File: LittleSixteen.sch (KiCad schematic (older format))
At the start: 17 parts

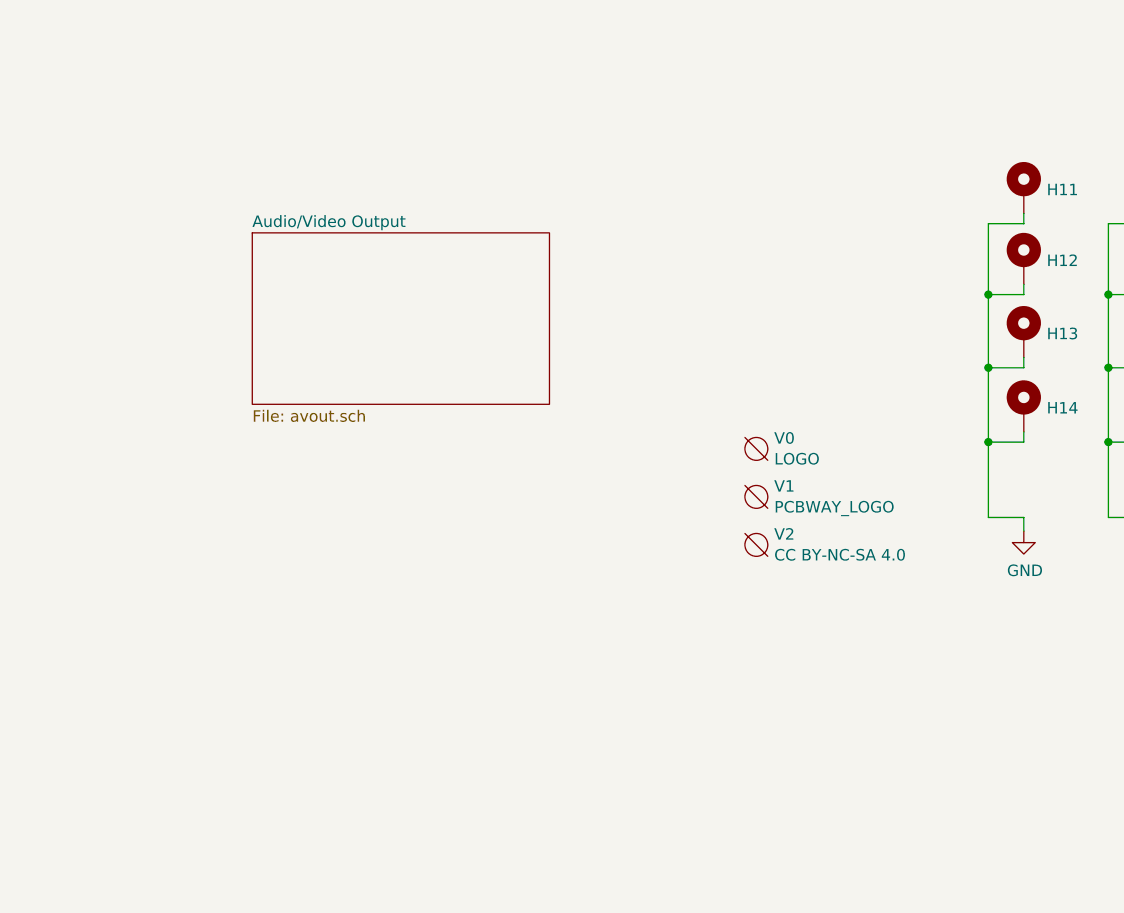
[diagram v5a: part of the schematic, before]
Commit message: Place components on board
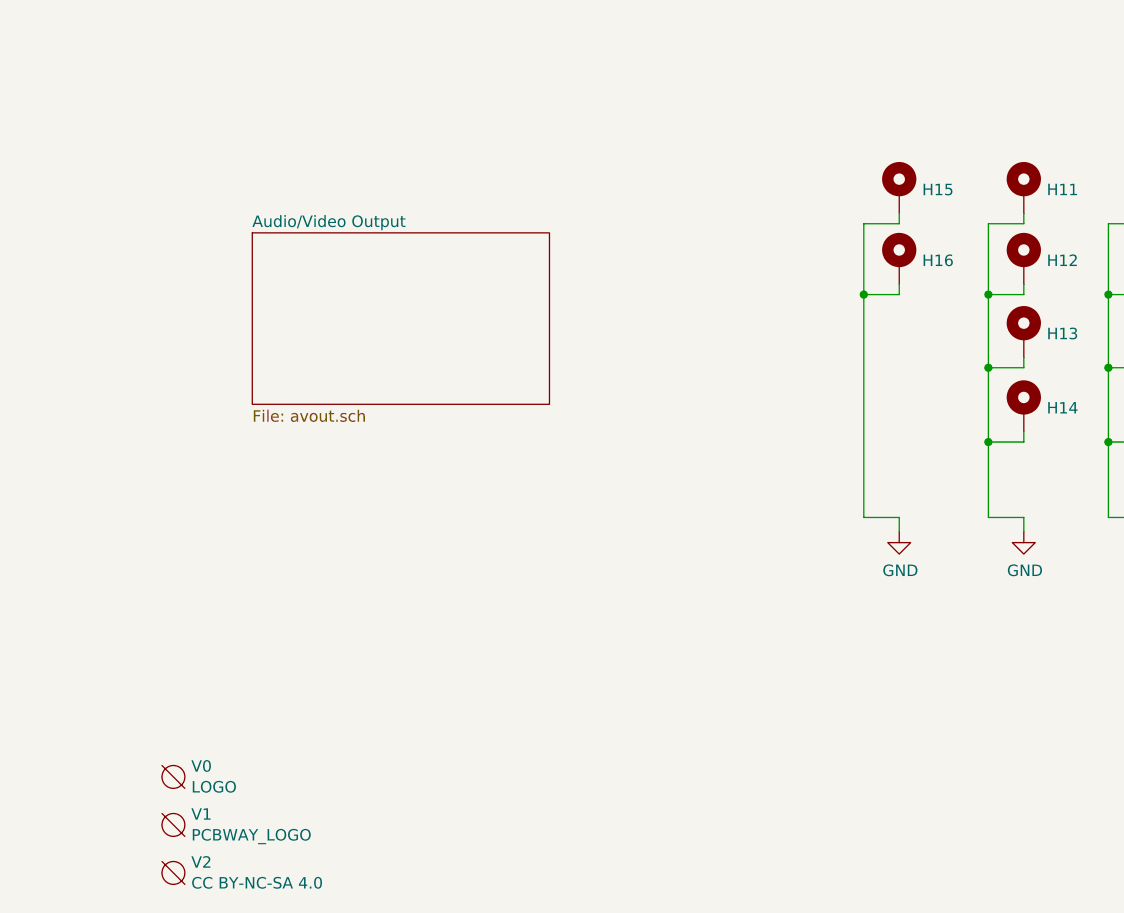
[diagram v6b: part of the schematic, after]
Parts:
- added H15, H16: MountingHole_Pad, MountingHole:MountingHole_3.7mm_Pad, symbol Mechanical:MountingHole_Pad
- H8: footprint MountingHole:MountingHole_4.3mm_M4_Pad -> (none)
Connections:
- net GND: now also H15.1, H16.1
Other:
- moved on the sheet: V0, V1, V2
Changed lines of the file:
@@
 F 0 "H8" H 10885 5563 50  0000 L CNN
 F 1 "MountingHole_Pad" H 10885 5518 50  0001 L CNN
-F 2 "MountingHole:MountingHole_4.3mm_M4_Pad" H 10785 5560 50  0001 C CNN
+F 2 "" H 10785 5560 50  0001 C CNN
 F 3 "~" H 10785 5560 50  0001 C CNN
 	1    10785 5560
@@
 L void:Void V0
 U 1 1 61145DF1
-P 8580 5735
-F 0 "V0" H 8658 5781 50  0000 L CNN
-F 1 "LOGO" H 8658 5690 50  0000 L CNN
-F 2 "LittleSixteen:Logo" H 8580 5735 50  0001 C CNN
-F 3 "" H 8580 5735 50  0001 C CNN
-	1    8580 5735
+P 6030 7170
+F 0 "V0" H 6108 7216 50  0000 L CNN
+F 1 "LOGO" H 6108 7125 50  0000 L CNN
+F 2 "LittleSixteen:Logo" H 6030 7170 50  0001 C CNN
+F 3 "" H 6030 7170 50  0001 C CNN
+	1    6030 7170
 	1    0    0    -1
 $EndComp
@@
 L void:Void V2
 U 1 1 61992CC0
-P 8580 6155
-F 0 "V2" H 8658 6201 50  0000 L CNN
-F 1 "CC BY-NC-SA 4.0" H 8658 6110 50  0000 L CNN
-F 2 "LittleSixteen:cc_by_nc_sa" H 8580 6155 50  0001 C CNN
-F 3 "" H 8580 6155 50  0001 C CNN
-	1    8580 6155
+P 6030 7590
+F 0 "V2" H 6108 7636 50  0000 L CNN
+F 1 "CC BY-NC-SA 4.0" H 6108 7545 50  0000 L CNN
+F 2 "LittleSixteen:cc_by_nc_sa" H 6030 7590 50  0001 C CNN
+F 3 "" H 6030 7590 50  0001 C CNN
+	1    6030 7590
 	1    0    0    -1
 $EndComp
@@
 L void:Void V1
 U 1 1 63408BAA
-P 8580 5945
-F 0 "V1" H 8658 5991 50  0000 L CNN
-F 1 "PCBWAY_LOGO" H 8658 5900 50  0000 L CNN
-F 2 "LittleSixteen:pcbway" H 8580 5945 50  0001 C CNN
-F 3 "" H 8580 5945 50  0001 C CNN
-	1    8580 5945
+P 6030 7380
+F 0 "V1" H 6108 7426 50  0000 L CNN
+F 1 "PCBWAY_LOGO" H 6108 7335 50  0000 L CNN
+F 2 "LittleSixteen:pcbway" H 6030 7380 50  0001 C CNN
+F 3 "" H 6030 7380 50  0001 C CNN
+	1    6030 7380
 	1    0    0    -1
 $EndComp
@@
 F1 "sid.sch" 50
 $EndSheet
+$Comp
+L Mechanical:MountingHole_Pad H15
+U 1 1 650CB05A
+P 9205 4605
+F 0 "H15" H 9305 4608 50  0000 L CNN
+F 1 "MountingHole_Pad" H 9305 4563 50  0001 L CNN
+F 2 "MountingHole:MountingHole_3.7mm_Pad" H 9205 4605 50  0001 C CNN
+F 3 "~" H 9205 4605 50  0001 C CNN
+	1    9205 4605
+	1    0    0    -1
+$EndComp
+$Comp
+L Mechanical:MountingHole_Pad H16
+U 1 1 650CB180
+P 9205 4915
+F 0 "H16" H 9305 4918 50  0000 L CNN
+F 1 "MountingHole_Pad" H 9305 4873 50  0001 L CNN
+F 2 "MountingHole:MountingHole_3.7mm_Pad" H 9205 4915 50  0001 C CNN
+F 3 "~" H 9205 4915 50  0001 C CNN
+	1    9205 4915
+	1    0    0    -1
+$EndComp
+Wire Wire Line
+	9050 6035 9205 6035
+Wire Wire Line
+	9205 6035 9205 6095
+$Comp
+L power:GND #PWR036
+U 1 1 650CB1A0
+P 9205 6095
+F 0 "#PWR036" H 9205 5845 50  0001 C CNN
+F 1 "GND" H 9210 5922 50  0000 C CNN
+F 2 "" H 9205 6095 50  0001 C CNN
+F 3 "" H 9205 6095 50  0001 C CNN
+	1    9205 6095
+	1    0    0    -1
+$EndComp
+Wire Wire Line
+	9205 5015 9205 5060
+Wire Wire Line
+	9205 5060 9050 5060
+Connection ~ 9050 5060
+Wire Wire Line
+	9205 4705 9205 4750
+Wire Wire Line
+	9205 4750 9050 4750
+Wire Wire Line
+	9050 4750 9050 5060
+Wire Wire Line
+	9050 5060 9050 6035
 $EndSCHEMATC

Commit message: Routing in progress
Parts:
- H5: footprint MountingHole:MountingHole_3.7mm_Pad -> (none)
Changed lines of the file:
@@
 F 0 "H5" H 10375 5238 50  0000 L CNN
 F 1 "MountingHole_Pad" H 10375 5193 50  0001 L CNN
-F 2 "MountingHole:MountingHole_3.7mm_Pad" H 10275 5235 50  0001 C CNN
+F 2 "" H 10275 5235 50  0001 C CNN
 F 3 "~" H 10275 5235 50  0001 C CNN
 	1    10275 5235
